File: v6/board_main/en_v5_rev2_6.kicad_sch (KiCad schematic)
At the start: 71 parts, among them J5 FEMALE_HEADER_2X1, U10 CY7C1051DV33, U9 S25FL256S, X2 32MHz, X3 100MHz

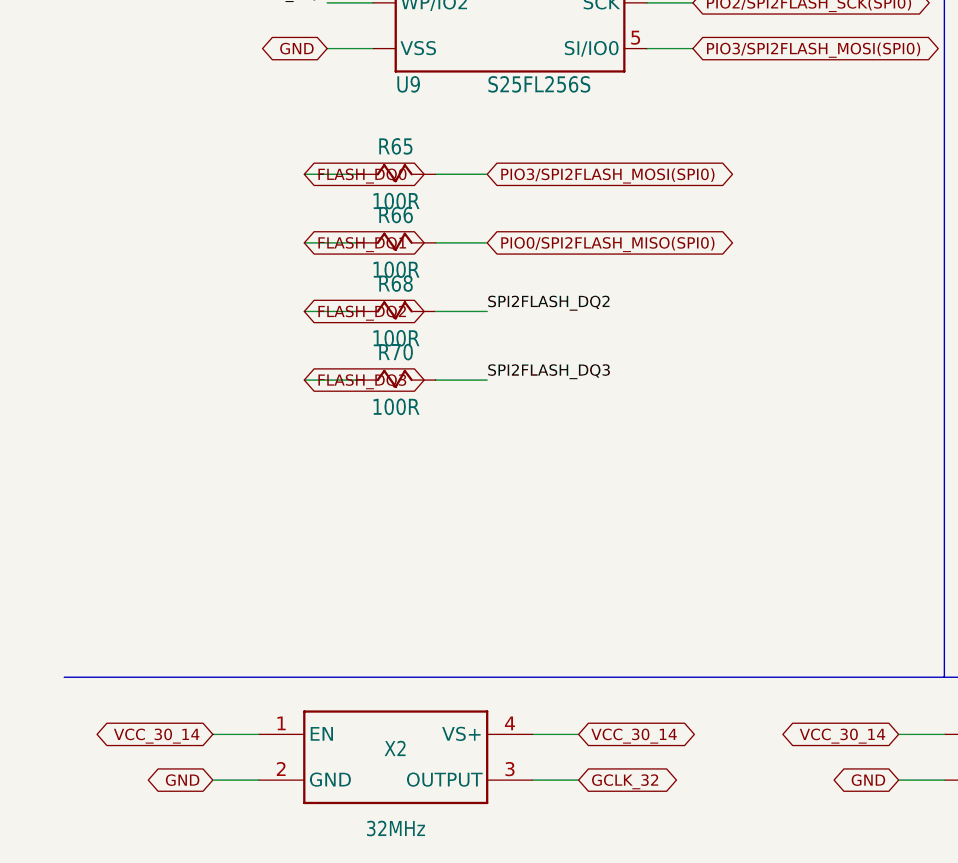
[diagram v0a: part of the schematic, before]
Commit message: Rephrasing ENV5 design
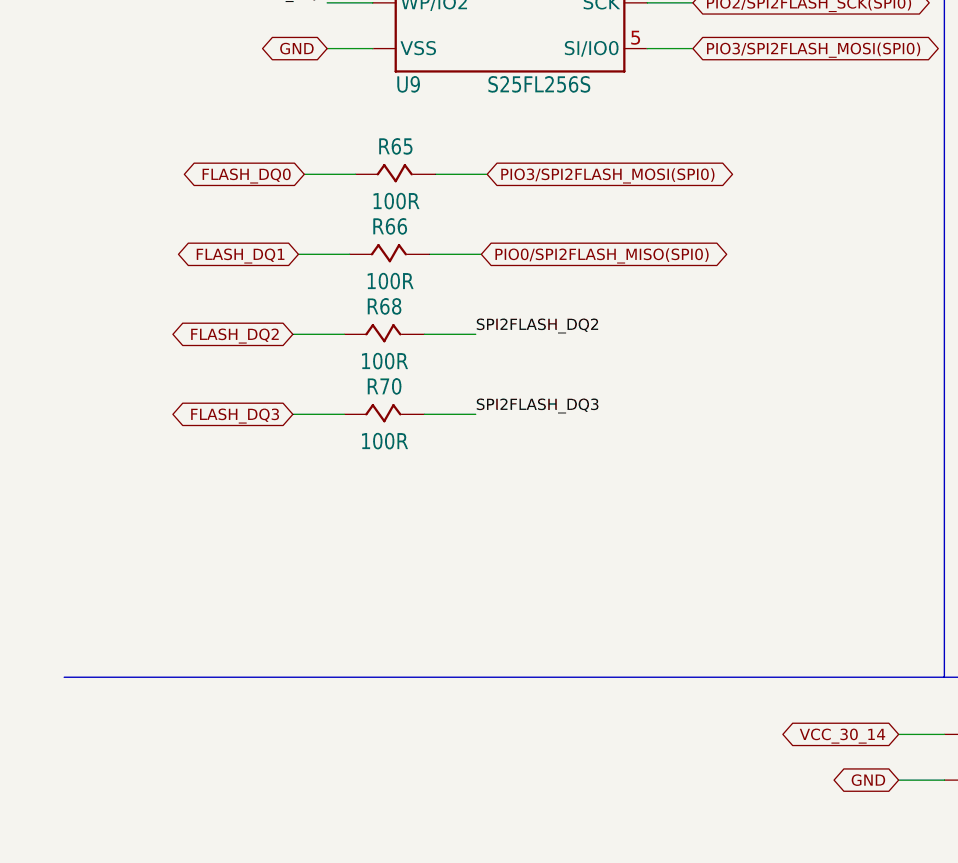
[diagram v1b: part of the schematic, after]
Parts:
- removed X2: 32MHz, env:3.2X2.5_OSC, symbol env-eagle-import:OSCILLATOR3.2X2.5
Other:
- moved on the sheet: R66, R68, R70
